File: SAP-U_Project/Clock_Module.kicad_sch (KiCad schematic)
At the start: 18 parts, among them SW2 SW_Push, U13 LM555xN, U15 ADG419BN, U3 LM555xN, U6 LM555xN

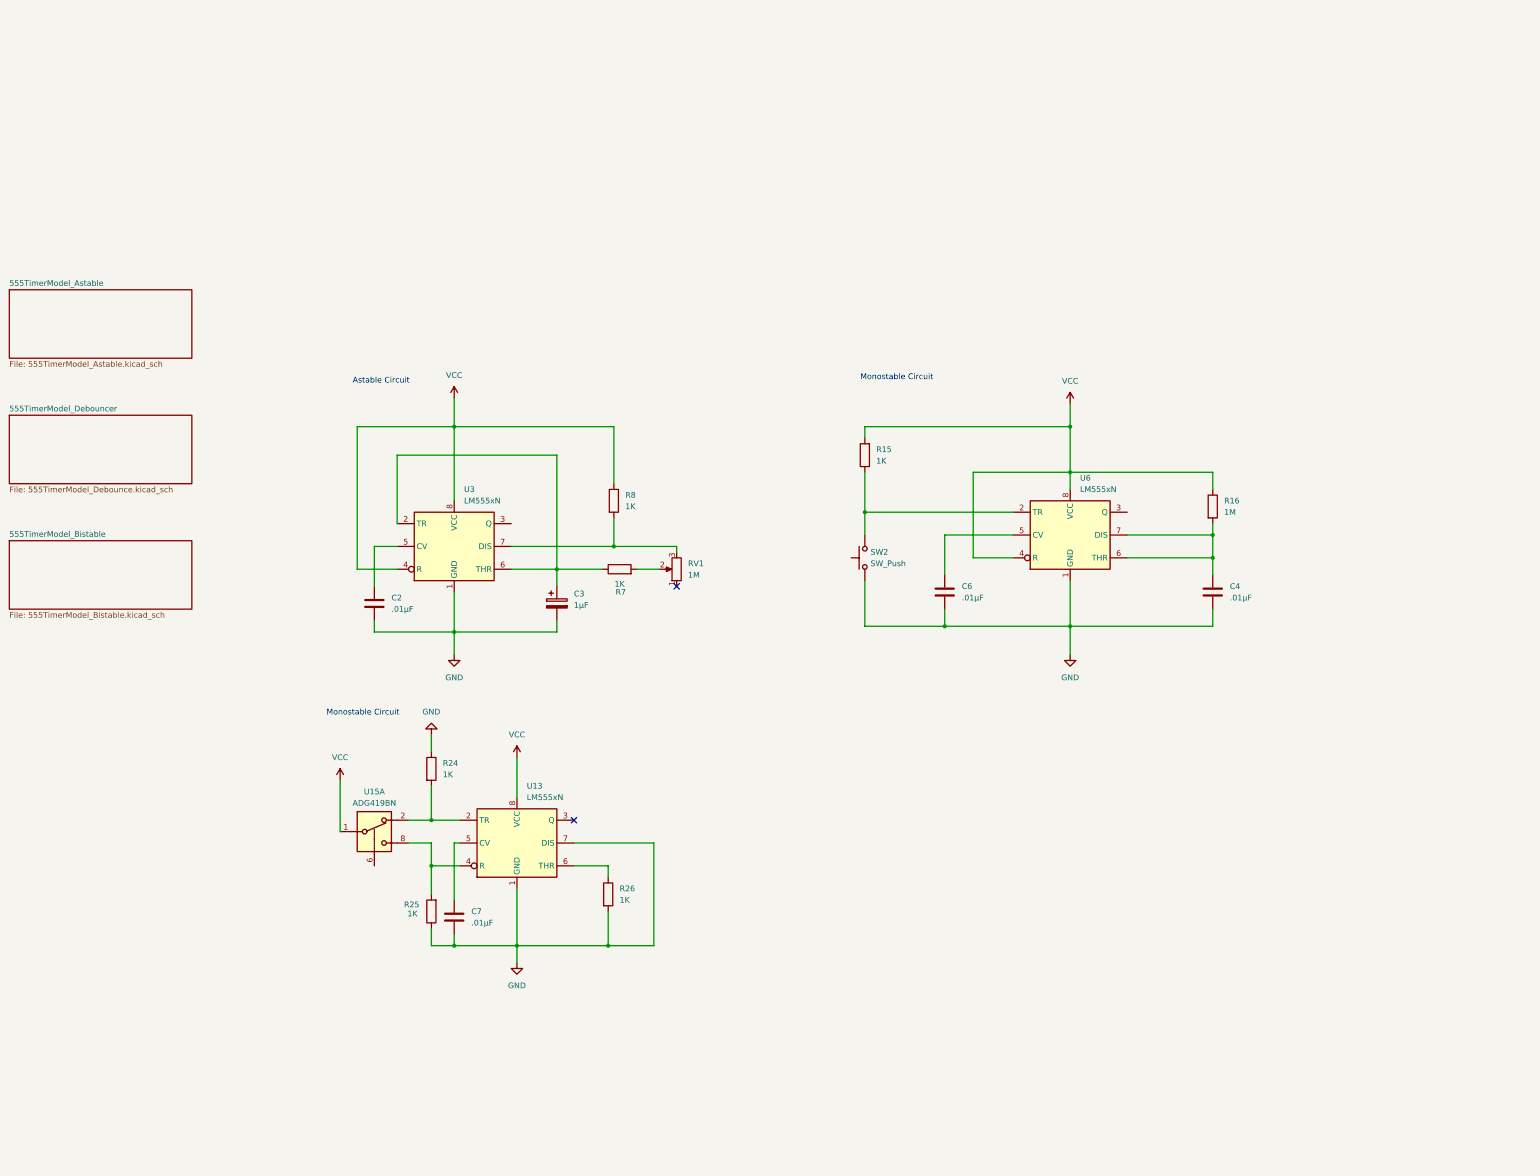
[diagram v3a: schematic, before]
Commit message: Checkpoint: added switching logic
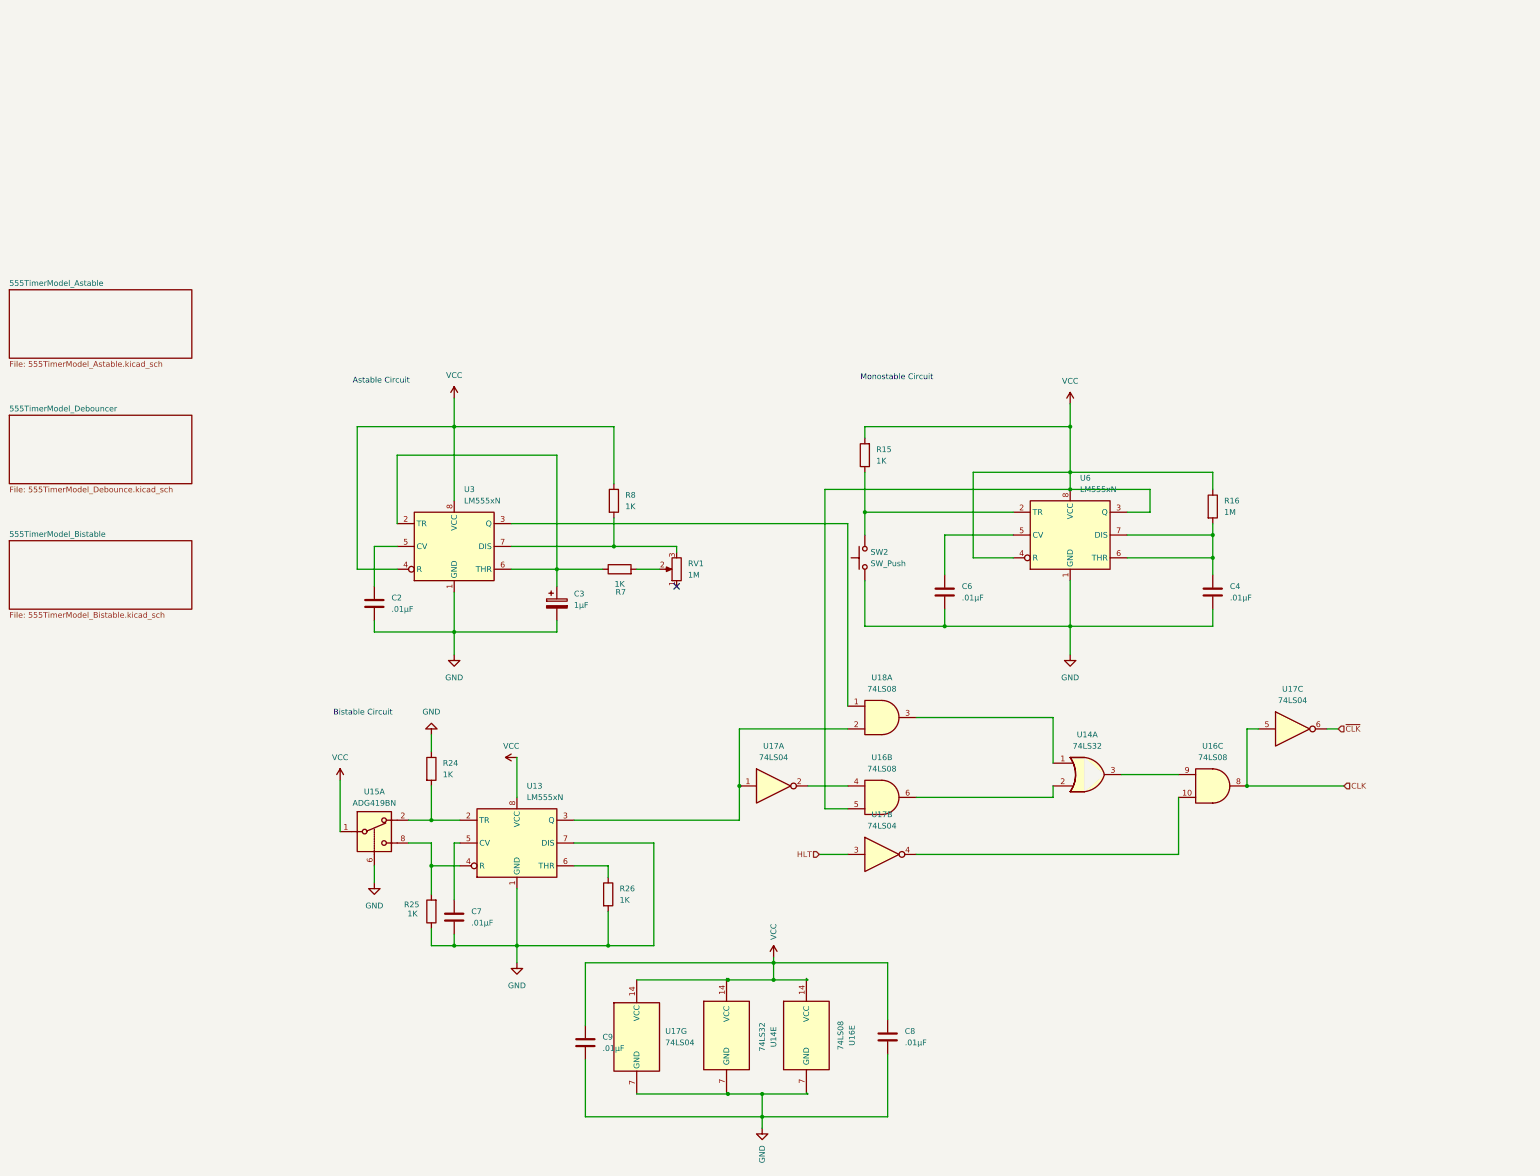
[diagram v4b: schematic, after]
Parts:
- added C8, C9: .01µF, symbol Device:C
- added U14: 74LS32, symbol 74xx:74LS32
- added U16, U18: 74LS08, symbol 74xx:74LS08
- added U17: 74LS04, symbol 74xx:74LS04
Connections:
- net GND: now also U15.6, C8.1, C9.1, U14.7 (GND), U16.7 (GND), U17.7 (GND)
- net VCC: now also U6.3 (Q), C8.2, C9.2, U14.14 (VCC), U16.14 (VCC), U16.5, U17.14 (VCC)
- net at U13.3 (Q): now also U17.1, U18.2
- net at U3.3 (Q): now also U18.1
- new net: U16.10, U17.4
- new net: U14.3, U16.9
- new net: U16.4, U17.2
- new net: U14.1, U18.3
- new net: U14.2, U16.6
- new net CLK: U16.8, U17.5
- new net HLT: U17.3
- new net ~{CLK}: U17.6
- no-connect marks 2 -> 1
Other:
- note added: "Bistable Circuit"

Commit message: Checkpoint: fixed ERC errors
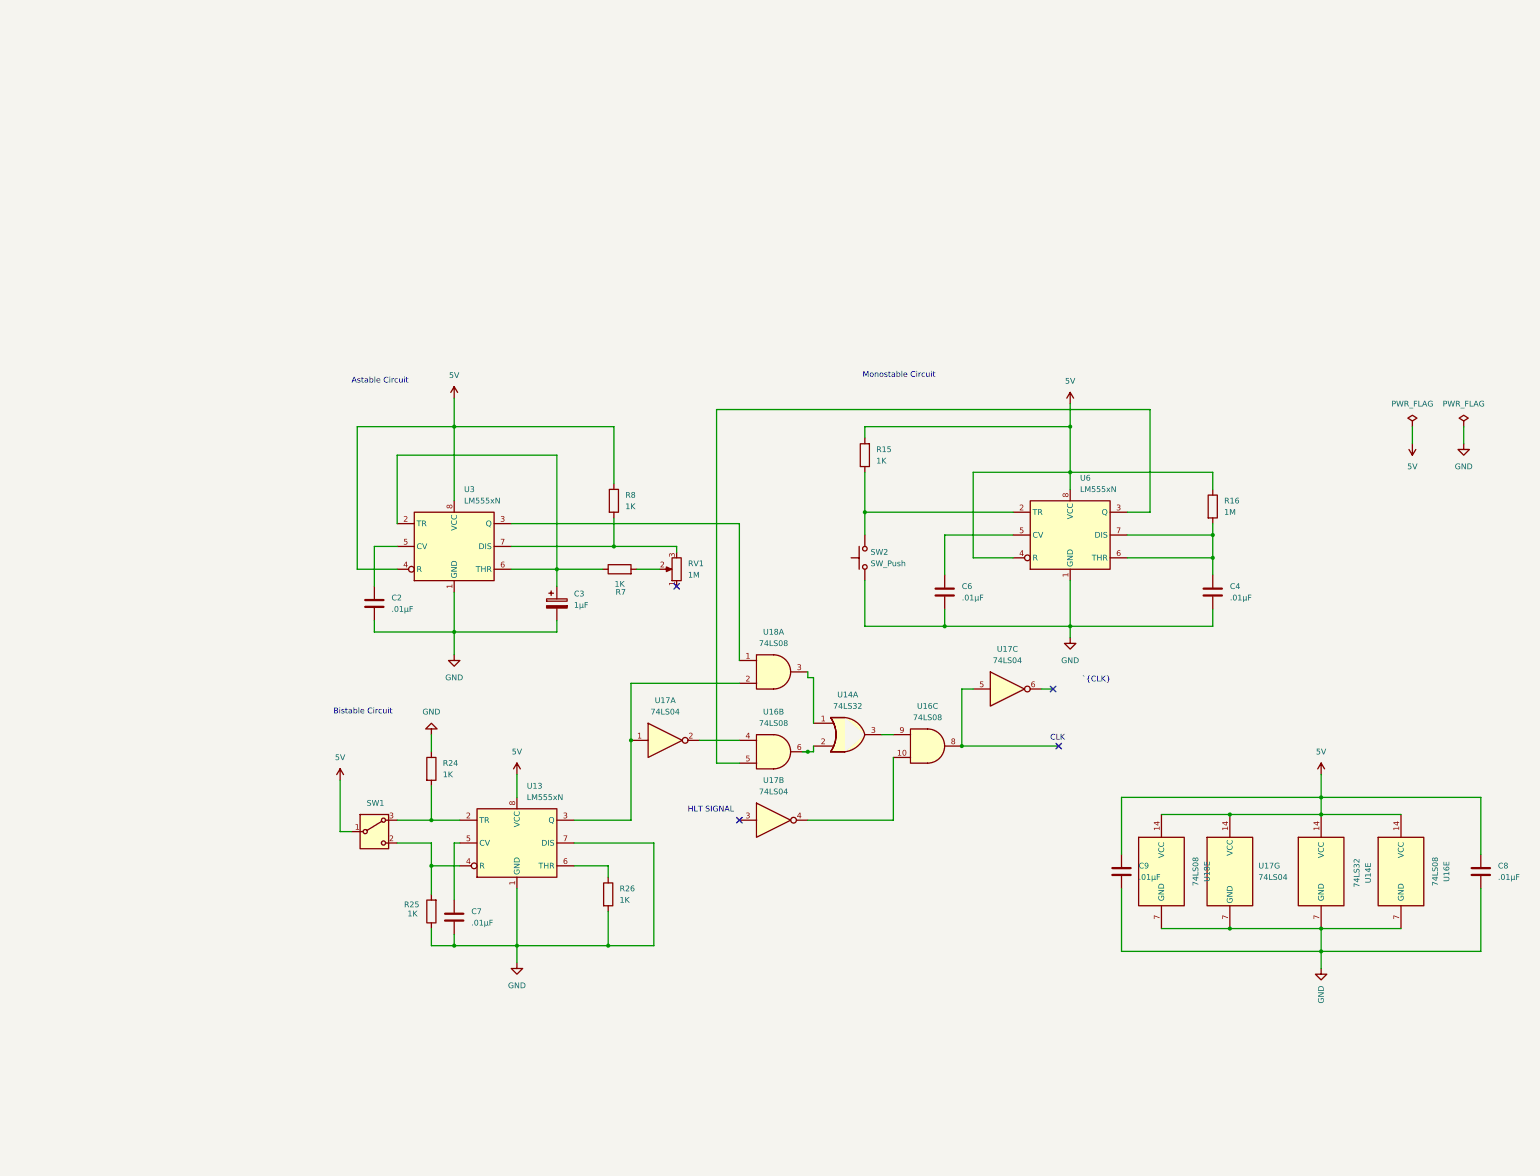
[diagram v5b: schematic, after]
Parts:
- removed U15: ADG419BN, Package_DIP:DIP-8_W7.62mm, symbol Analog_Switch:ADG419BN
- added SW1: SW_Wuerth_450301014042, Button_Switch_THT:SW_Slide-03_Wuerth-WS-SLTV_10x2.5x6.4_P2.54mm, symbol Switch:SW_Wuerth_450301014042
- added unit 5 of U18
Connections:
- net GND: now also U18.7 (GND)
- net at R24.2, U13.2 (TR): now also SW1.3 (A)
- net at R25.2, U13.4 (R): now also SW1.2 (C)
- net CLK: no longer names the net of U16.8, U17.5
- net HLT: no longer names the net of U17.3
- net VCC renamed 5V
- net 5V: now also SW1.1 (B), U18.14 (VCC); no longer U16.5, U6.3 (Q)
- net ~{CLK}: no longer names the net of U17.6
- new net: U16.5, U6.3 (Q)
- no-connect marks 1 -> 4
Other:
- removed sheet 555TimerModel_Astable
- removed sheet 555TimerModel_Bistable
- removed sheet 555TimerModel_Debouncer
- note added: "CLK"
- note added: "HLT SIGNAL"
- note added: "`{CLK}"
- moved on the sheet: C8, C9, U14A, U14E, U16B, U16C, U16E, U17A, U17B, U17C, U17G, U18A

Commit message: cleaned up circuit for bistable, monostable, and astable circuits
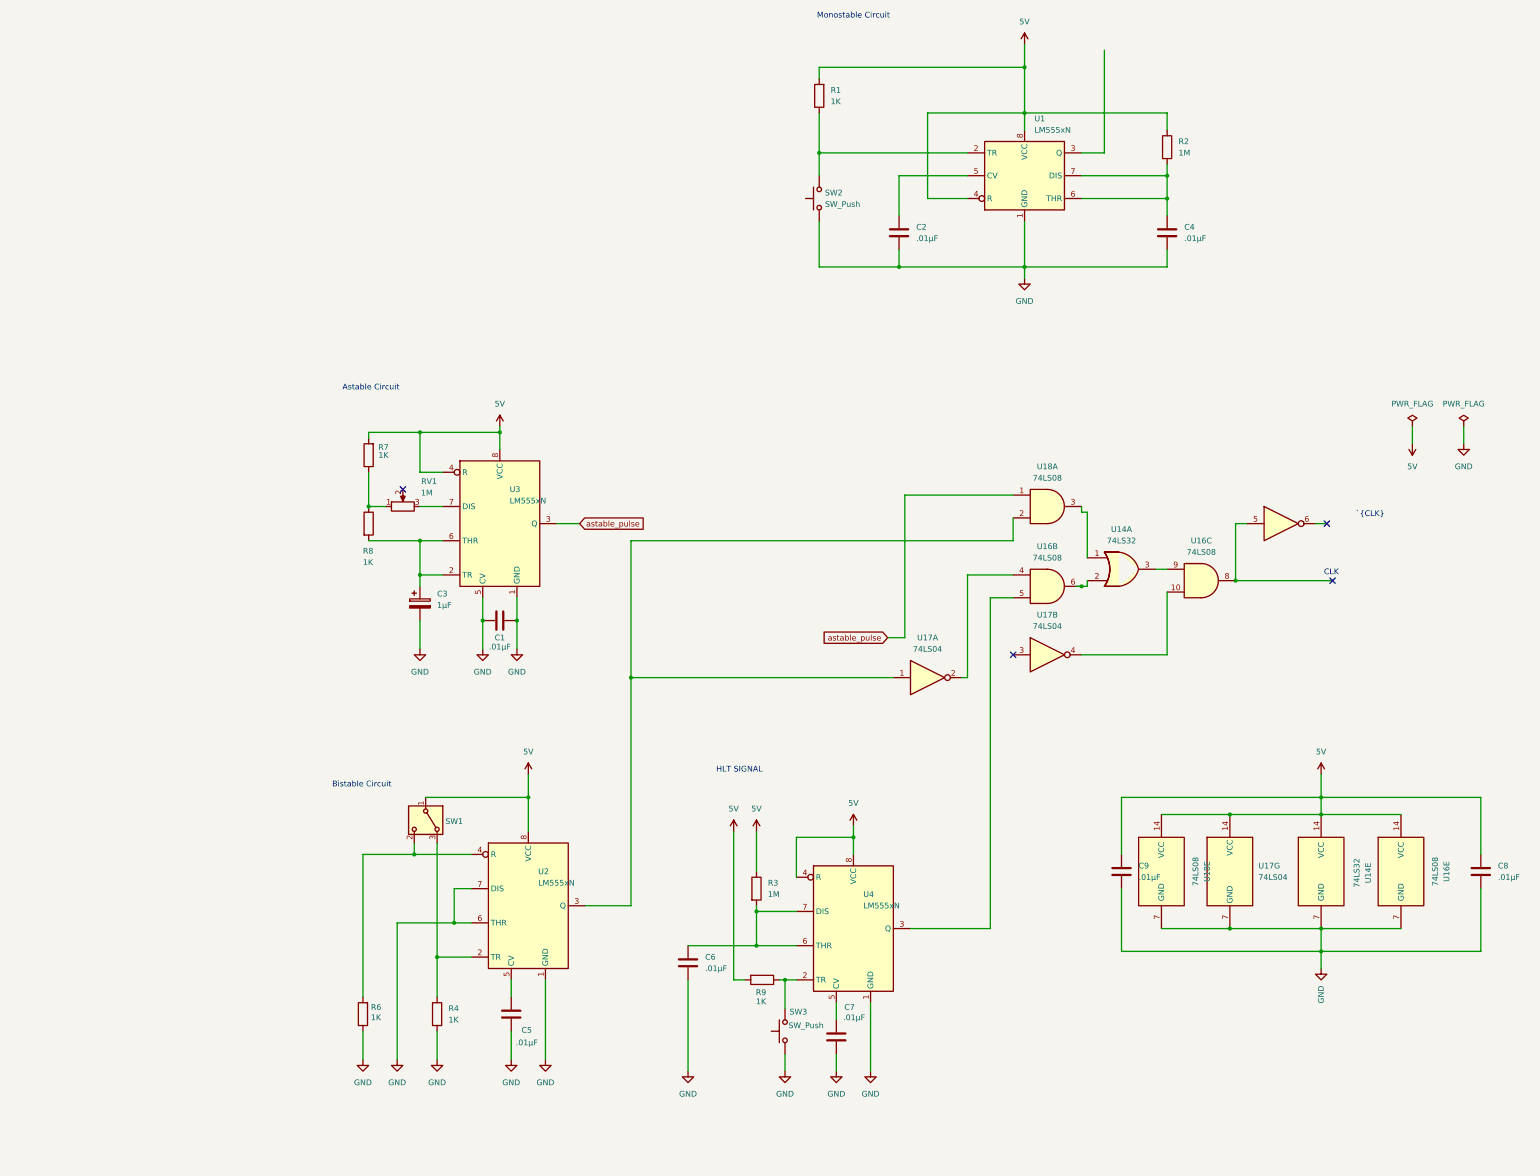
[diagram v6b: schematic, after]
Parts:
- removed R15, R24, R25, R26: 1K, symbol Device:R
- removed R16: 1M, symbol Device:R
- removed U13, U6: LM555xN, Package_DIP:DIP-8_W7.62mm, symbol Timer:LM555xN
- added C1, C5: .01µF, symbol Device:C
- added R1, R4, R6, R9: 1K, symbol Device:R
- added R2, R3: 1M, symbol Device:R
- added SW3: SW_Push, symbol Switch:SW_Push
- added U1, U2, U4: LM555xN, Package_DIP:DIP-8_W7.62mm, symbol Timer:LM555xN
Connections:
- net 5V: now also R7.2, R1.2, R2.1, R3.1, R9.2, U1.4 (R), U1.8 (VCC), U2.8 (VCC), U4.4 (R), U4.8 (VCC); no longer R8.1
- net GND: now also U3.5 (CV), C1.1, C1.2, C5.1, R4.2, R6.1, SW3.1, U1.1 (GND), U2.1 (GND), U2.6 (THR), U2.7 (DIS), U4.1 (GND)
- net at SW2.2: now also R1.1, U1.2 (TR)
- net at SW1.3 (A): now also R4.1, U2.2 (TR)
- net at U17.1, U18.2: now also U2.3 (Q)
- net at SW1.2 (C): now also R6.2, U2.4 (R)
- net at C7.2: now also U4.5 (CV)
- net at C6.2: now also R3.2, U4.6 (THR), U4.7 (DIS)
- net at C4.2: now also R2.2, U1.6 (THR), U1.7 (DIS)
- net astable_pulse: now reaches U18.1, U3.3 (Q)
- net at RV1.3, U3.7 (DIS): no longer R8.2
- net at C3.1, U3.2 (TR), U3.6 (THR): now also R8.2; no longer R7.1
- net at RV1.2: no longer R7.2
- net at RV1.1: now also R7.1, R8.1
- net at C2.2: now also U1.5 (CV); no longer U3.5 (CV)
- net at U16.5: now also U4.3 (Q)
- new net: C5.2, U2.5 (CV)
- new net: R9.1, SW3.2, U4.2 (TR)
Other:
- moved on the sheet: C3, R7, R8, RV1, U14A, U16B, U16C, U17A, U17B, U18A, U3

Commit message: Checkpoint: completed schematic for Clock Module
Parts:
- removed C2, C4, C8, C9: .01µF, symbol Device:C
- removed R1: 1K, symbol Device:R
- removed R2: 1M, symbol Device:R
- removed RV1: 1M, symbol Device:R_Potentiometer
- removed SW2: SW_Push, symbol Switch:SW_Push
- removed U1: LM555xN, Package_DIP:DIP-8_W7.62mm, symbol Timer:LM555xN
- removed U14: 74LS32, symbol 74xx:74LS32
- removed U16, U18: 74LS08, symbol 74xx:74LS08
- removed U17: 74LS04, symbol 74xx:74LS04
- added D1: LED, symbol Device:LED
- added POT1: 1M, symbol Device:R_Potentiometer
- added R7: 1K, symbol Device:R
- added U1: 74LS08, symbol 74xx:74LS08
- added U5: 74LS32, symbol 74xx:74LS32
- added U6: 74LS04, symbol 74xx:74LS04
- renumbered C3 to C1, C1 to C2, C6 to C3, C7 to C4, C5 to C6, SW3 to Push1, R7 to R1, R8 to R2, R9 to R4, R6 to R5, R4 to R6
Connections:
- net 5V: now also U1.14 (VCC), U5.14 (VCC), U6.14 (VCC)
- net GND: now also R7.2, U1.7 (GND), U5.7 (GND), U6.7 (GND)
- net bistable_out: now reaches U2.3 (Q)
- net bistable_out: now also U1.2, U6.1
- net at R1.1, R2.1: now also U3.7 (DIS)
- net at C1.1, U3.2 (TR), U3.6 (THR): now also POT1.3; no longer R2.2
- net monostable_out: now reaches U4.3 (Q)
- net monostable_out: now also U1.5
- net astable_pulse renamed astable_out
- net astable_out: now also U1.1
- new net: U1.10, U6.4
- new net: U1.9, U5.3
- new net: POT1.1, R2.2
- new net: U1.4, U6.2
- new net: U1.6, U5.2
- new net: D1.1 (K), R7.1
- new net: U1.3, U5.1
- new net CLK: D1.2 (A), U1.8, U6.5
- new net ~{CLK}: U6.6
- no-connect marks 4 -> 2
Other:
- note added: "Change to HLT"
- note removed: "CLK"
- note removed: "HLT SIGNAL"
- note removed: "`{CLK}"
- moved on the sheet: C1, C2, C3, C4, C6, Push1, R1, R2, R3, R4, R5, R6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
